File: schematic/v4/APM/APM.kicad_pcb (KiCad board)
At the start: 4 copper layers, 72.5 x 104.5 mm, 74 parts, among them J1 ACM_CTRL, J11 INA219_CONFIG, J12 AUDIO_OUT, J13 Conn_02x36_Odd_Even, J15 Conn_02x36_Odd_Even, J2 CAN, J21 USB_A, J29 USB_A, J3 7SDD_CTRL, J30 UART_DEBUG, J4 LCD_display, J5 INTRPT, J7 TDM_PMS_I2C, SW1 WARN_RST, SW2 FAIL_RST, U1 NUCLEO-H753ZI, U13 INA219AxD, U38 CH340G, Y7 12MHz

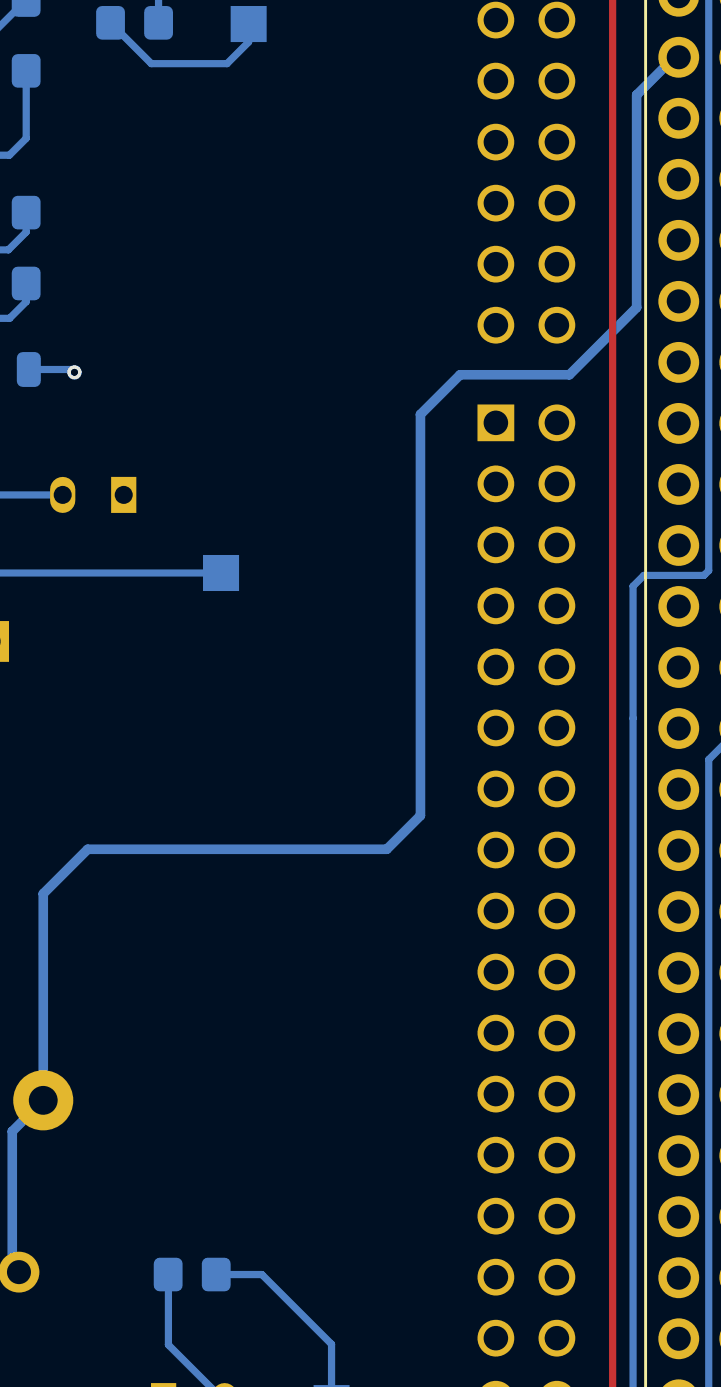
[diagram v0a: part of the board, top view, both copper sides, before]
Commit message: gonna use a 10 pin FFC to connect to the actual peripheral board
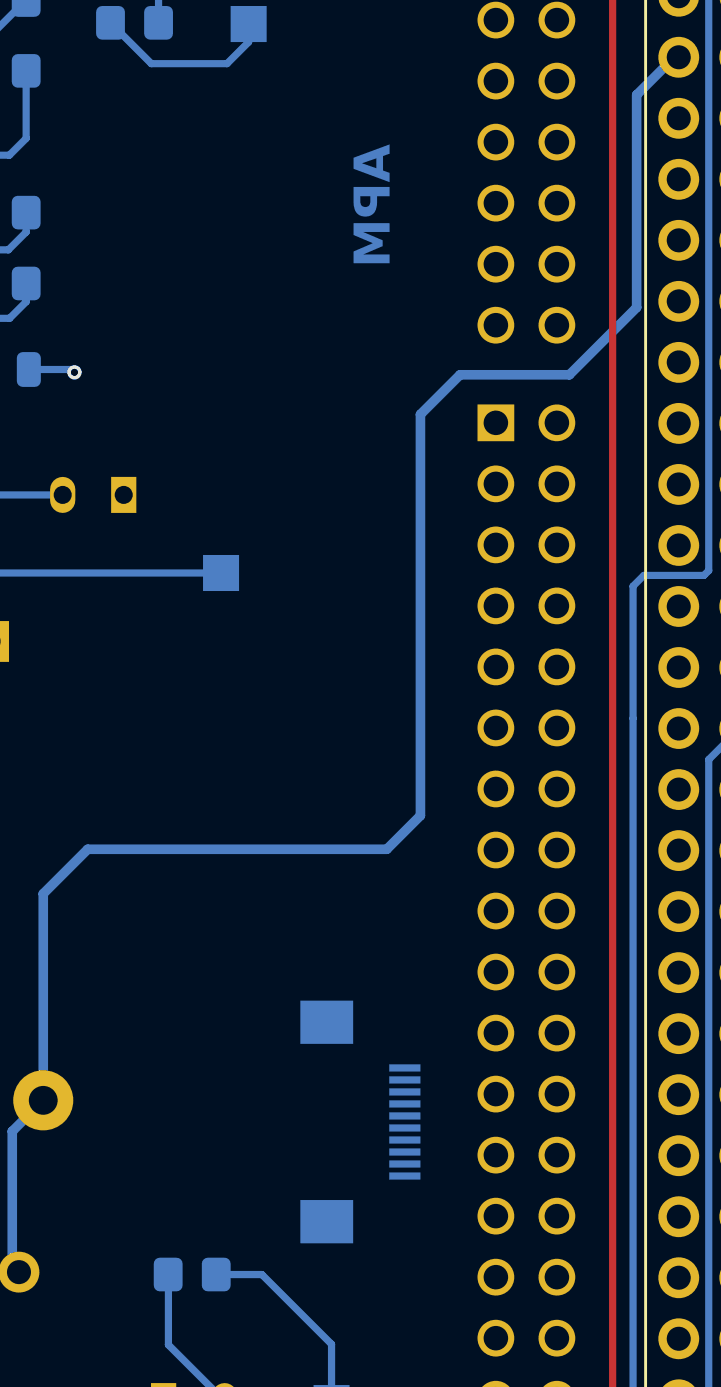
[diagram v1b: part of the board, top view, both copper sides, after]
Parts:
- added J14: periperhals, Connector_FFC-FPC:Hirose_FH12-10S-0.5SH_1x10-1MP_P0.50mm_Horizontal, B.Cu at (112.7, 119.7)
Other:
- board text added: "APM"

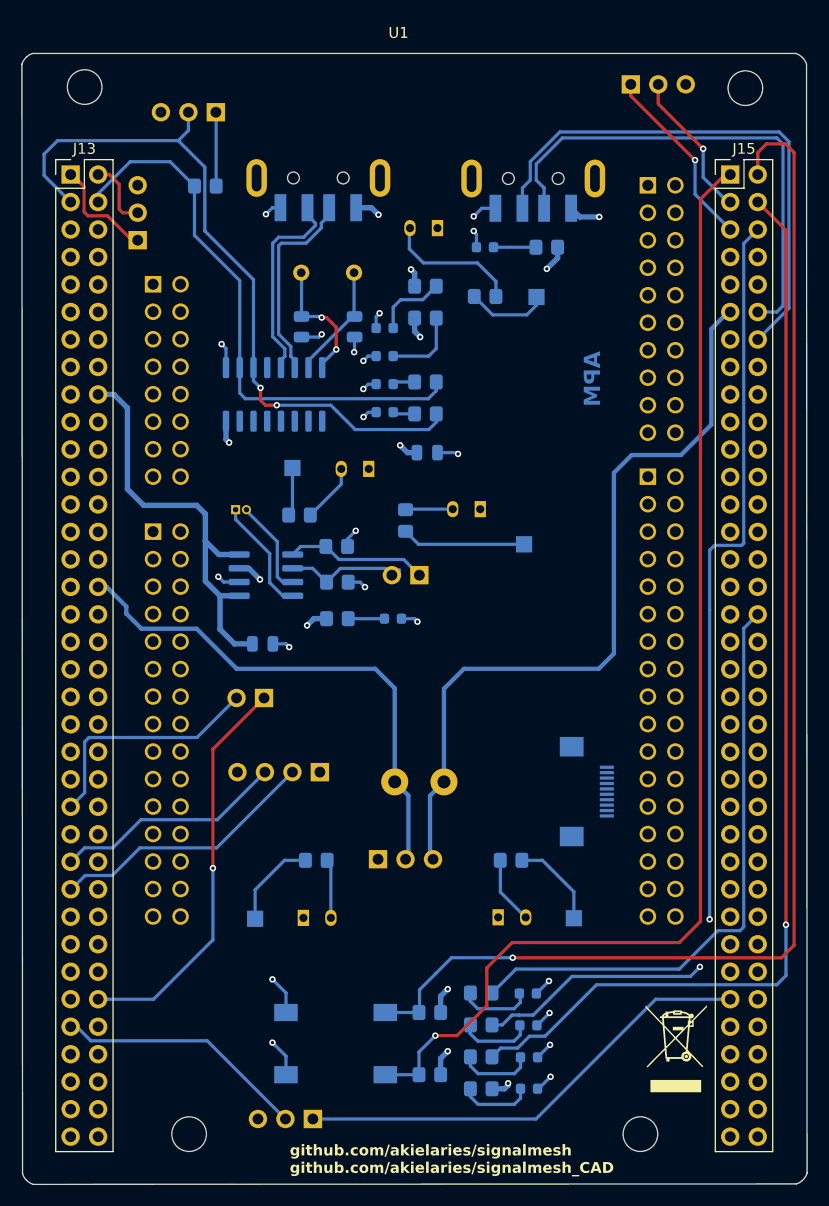
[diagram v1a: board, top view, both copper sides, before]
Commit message: voltage divider
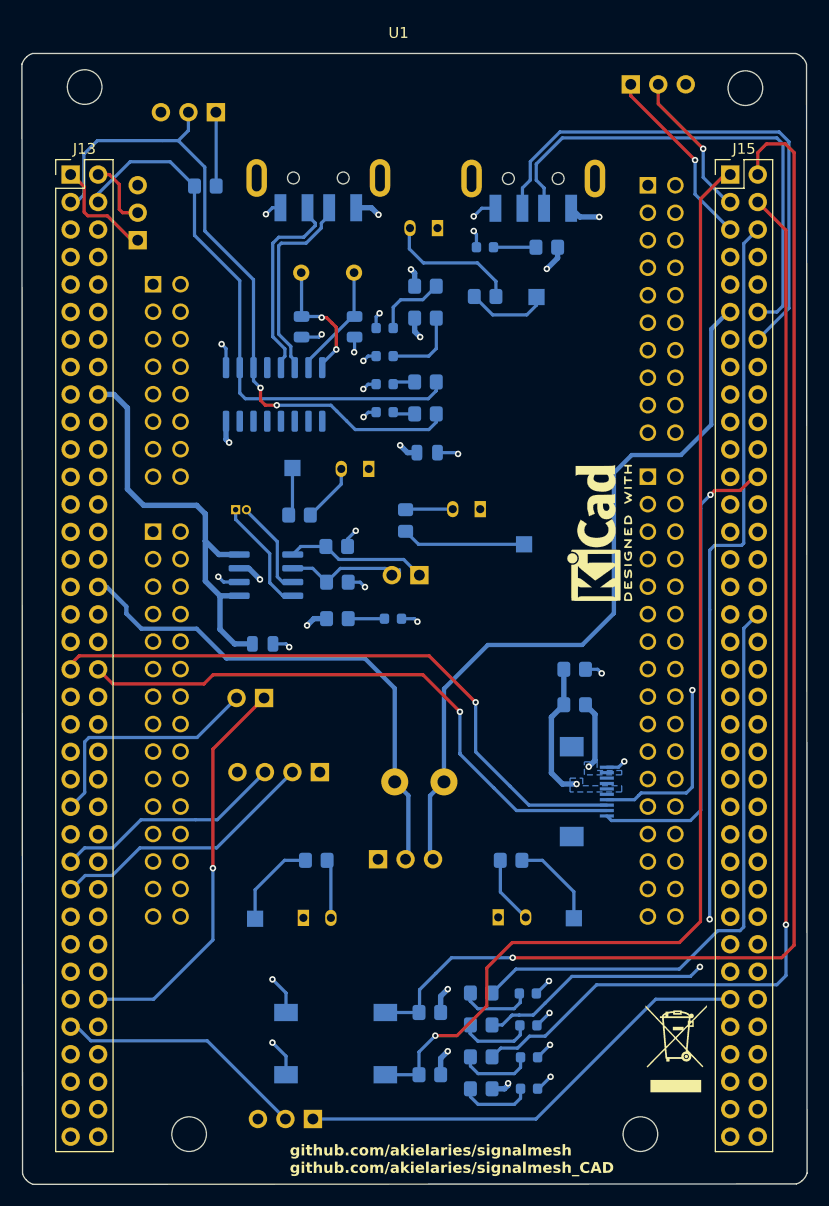
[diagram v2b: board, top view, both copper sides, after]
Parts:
- added R3: 10k, Resistor_SMD:R_0805_2012Metric_Pad1.20x1.40mm_HandSolder, B.Cu at (111.5, 111.6)
- added R4: 20k, Resistor_SMD:R_0805_2012Metric_Pad1.20x1.40mm_HandSolder, B.Cu at (111.5, 108.3)
- REF**: moved to F.Cu
- moved REF** 51.6 mm to (73.0, 136.4)
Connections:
- J13 pad 16: unconnected-(J13-Pin_16-Pad16) -> 3V3_APM_MCU
- J13 pad 37: unconnected-(J13-Pin_37-Pad37) -> /POT_3
- J13 pad 38: unconnected-(J13-Pin_38-Pad38) -> /POT_2
- J14 pad 1: unconnected-(J14-Pin_1-Pad1) -> /POT_1
- J14 pad 10: unconnected-(J14-Pin_10-Pad10) -> GND
- J14 pad 2: unconnected-(J14-Pin_2-Pad2) -> /POT_2
- J14 pad 3: unconnected-(J14-Pin_3-Pad3) -> /POT_3
- J14 pad 4: unconnected-(J14-Pin_4-Pad4) -> /POT_4
- J14 pad 6: unconnected-(J14-Pin_6-Pad6) -> /3V3_APM
- J14 pad 9: unconnected-(J14-Pin_9-Pad9) -> 5V_APM
- J15 pad 24: unconnected-(J15-Pin_24-Pad24) -> /POT_1
- J15 pad 37: unconnected-(J15-Pin_37-Pad37) -> /POT_4
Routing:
- net /POT_3: track 0.00 -> 58.7 mm, vias 0 -> 1
- net /POT_2: track 0.00 -> 55.4 mm, vias 0 -> 1
- net /POT_1: track 0.00 -> 43.8 mm, vias 0 -> 1
- net /POT_4: track 0.00 -> 21.6 mm, vias 0 -> 1
- net /3V3_APM: track 0.00 -> 12.5 mm, vias 0 -> 1
- net 5V_APM: track 26.3 -> 32.7 mm, vias 12 -> 13
- net /APM_DBG_TX: track 67.4 -> 63.1 mm
- net GND: track 41.2 -> 44.7 mm, vias 22 -> 24
- net /APM_DAC_L: track 72.2 -> 70.1 mm
- added copper zone on B.Cu, net /3V3_APM
- added copper zone on B.Cu, net 5V_APM
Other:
- board text added: "___ ____ __ ___ / | / __ \/ |/ / / /| | / /_/ / /|_/ / / ___ |/ ____/ / / / /_/ |_/_/ /_/ /_/"
- board text removed: "APM"

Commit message: this seems good enough
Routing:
- net /3V3_APM: track 12.5 -> 15.9 mm, vias 1 -> 2
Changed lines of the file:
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@@
 			(pinfunction "Pin_5")
 			(pintype "passive+no_connect")
+			(clearance 0.01)
 		)
 		(pad "6" smd rect
@@
 			(pinfunction "Pin_7")
 			(pintype "passive+no_connect")
+			(clearance 0.01)
 		)
 		(pad "8" smd rect
@@
 			(pinfunction "Pin_10")
 			(pintype "passive")
+			(clearance 0.01)
 		)
 		(pad "MP" smd rect
@@
 		(net 64)
 	)
+	(segment
+		(start 110.825 117.35)
+		(end 109.4 117.35)
+		(width 0.5)
+		(layer "F.Cu")
+		(net 122)
+	)
+	(segment
+		(start 109.4 117.35)
+		(end 109.375 117.35)
+		(width 0.5)
+		(layer "F.Cu")
+		(net 122)
+	)
+	(segment
+		(start 111.7 118.225)
+		(end 111.05 117.575)
+		(width 0.5)
+		(layer "F.Cu")
+		(net 122)
+	)
+	(segment
+		(start 111.05 117.575)
+		(end 110.825 117.35)
+		(width 0.5)
+		(layer "F.Cu")
+		(net 122)
+	)
+	(segment
+		(start 111.7 118.95)
+		(end 111.7 118.225)
+		(width 0.5)
+		(layer "F.Cu")
+		(net 122)
+	)
 	(via
-		(at 111.7 118.95)
+		(at 109.4 117.35)
 		(size 0.6)
 		(drill 0.3)
@@
 		(net 122)
 	)
-	(segment
-		(start 111.7 118.95)
-		(end 110.4 118.95)
-		(width 0.5)
-		(layer "B.Cu")
+	(via
+		(at 111.7 118.95)
+		(size 0.6)
+		(drill 0.3)
+		(layers "F.Cu" "B.Cu")
 		(net 122)
 	)
@@
 	)
 	(segment
+		(start 111.7 118.95)
+		(end 110.4 118.95)
+		(width 0.5)
+		(layer "B.Cu")
+		(net 122)
+	)
+	(segment
 		(start 84 83.95)
 		(end 82.95 83.95)
@@
 		(polygon
 			(pts
-				(xy 115.875 118.1) (xy 112.425 118.1) (xy 112.425 116.9) (xy 113.6 116.9) (xy 113.6 117.7) (xy 115.875 117.7)
+				(xy 115.875 118.125) (xy 112.425 118.125) (xy 112.425 116.9) (xy 113.6 116.9) (xy 113.6 117.65)
+				(xy 115.875 117.65)
 			)
 		)
@@
 		)
 	)
+	(group ""
+		(members "4d033f77-9997-4530-bc92-737d369a60b3" "737ecc42-4660-4a96-996d-9a2152231149"
+			"bfa9058a-683d-4c78-b3de-55686d417cfc" "f91d4b70-0b13-4208-92fc-98827bbd2906"
+		)
+	)
